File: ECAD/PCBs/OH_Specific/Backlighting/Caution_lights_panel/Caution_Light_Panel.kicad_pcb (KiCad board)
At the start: 2 copper layers, 81.9 x 39.8 mm, 31 parts, among them J1 Conn_01x04_Female, J2 Conn_01x04_Female

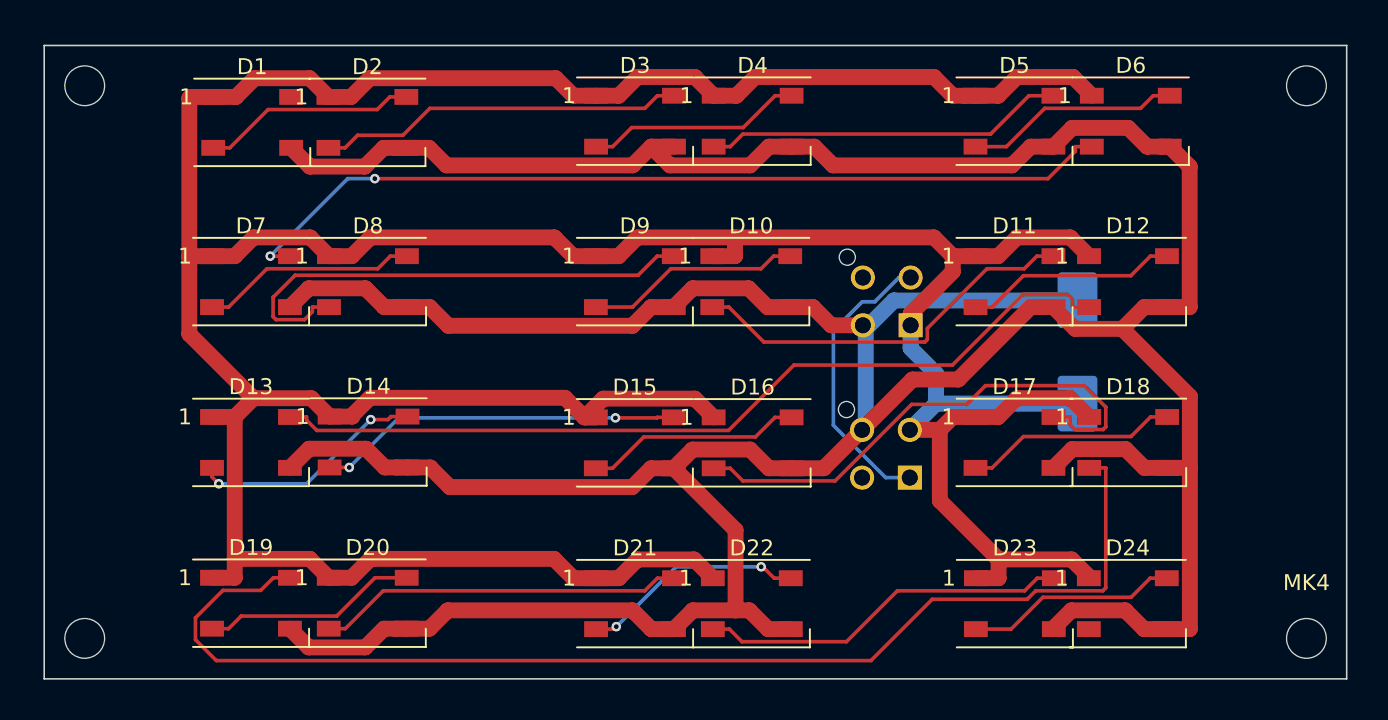
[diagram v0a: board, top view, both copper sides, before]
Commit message: Defog Lever Backlighting
Added - Degfog Lever PCB ECAD Files
Added - Defog Lever PCB MCAD Model
Added - Holes in the backplate for the backlighting LEDs
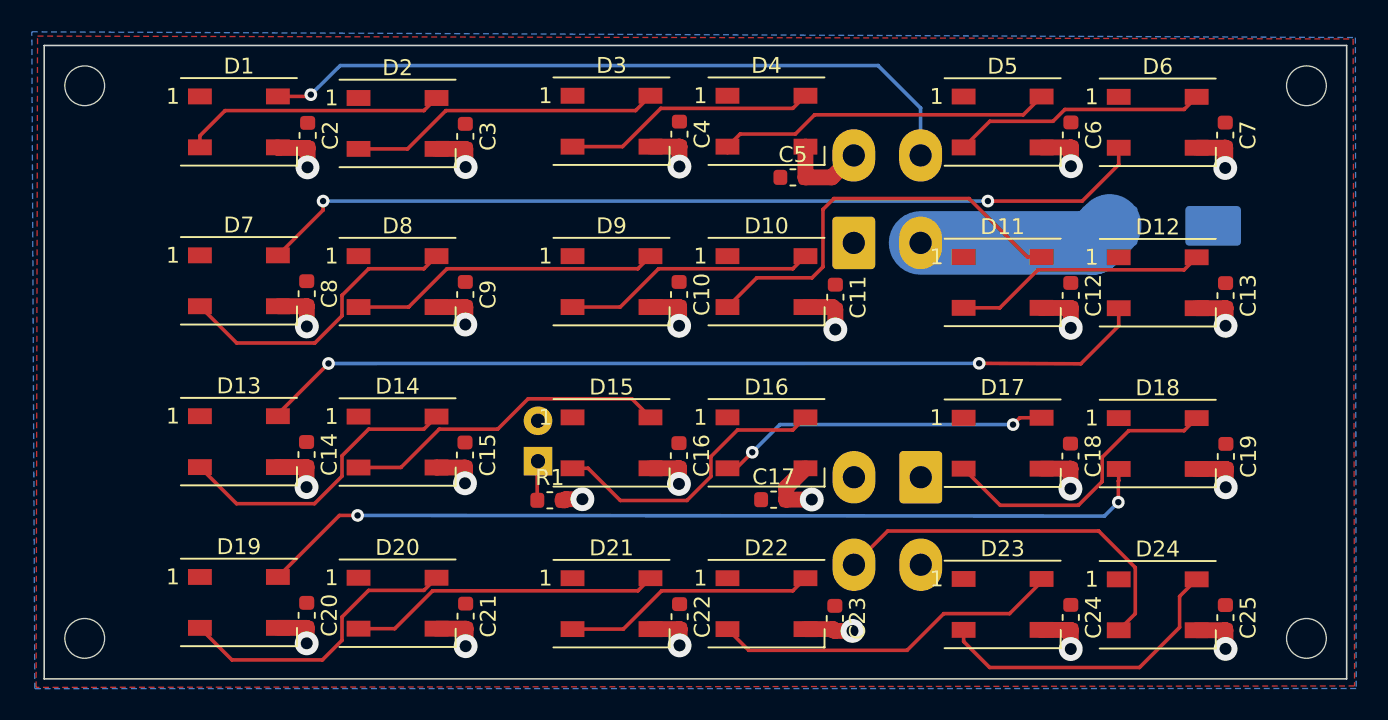
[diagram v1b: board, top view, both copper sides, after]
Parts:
- added C10: C, Capacitor_SMD:C_0603_1608Metric, F.Cu at (146.6, 85.7)
- added C11: C, Capacitor_SMD:C_0603_1608Metric, F.Cu at (156.4, 85.9)
- added C12: C, Capacitor_SMD:C_0603_1608Metric, F.Cu at (171.2, 85.8)
- added C13: C, Capacitor_SMD:C_0603_1608Metric, F.Cu at (180.9, 85.8)
- added C14: C, Capacitor_SMD:C_0603_1608Metric, F.Cu at (123.1, 95.8)
- added C15: C, Capacitor_SMD:C_0603_1608Metric, F.Cu at (133.1, 95.8)
- added C16: C, Capacitor_SMD:C_0603_1608Metric, F.Cu at (146.6, 95.9)
- added C17: C, Capacitor_SMD:C_0603_1608Metric, F.Cu at (152.5, 98.6)
- added C18: C, Capacitor_SMD:C_0603_1608Metric, F.Cu at (171.2, 95.9)
- added C19: C, Capacitor_SMD:C_0603_1608Metric, F.Cu at (180.9, 95.9)
- added C2: C, Capacitor_SMD:C_0603_1608Metric, F.Cu at (123.2, 75.7)
- added C20: C, Capacitor_SMD:C_0603_1608Metric, F.Cu at (123.2, 105.9)
- added C21: C, Capacitor_SMD:C_0603_1608Metric, F.Cu at (133.1, 105.9)
- added C22: C, Capacitor_SMD:C_0603_1608Metric, F.Cu at (146.6, 106.0)
- added C23: C, Capacitor_SMD:C_0603_1608Metric, F.Cu at (156.3, 106.1)
- added C24: C, Capacitor_SMD:C_0603_1608Metric, F.Cu at (171.2, 106.0)
- added C25: C, Capacitor_SMD:C_0603_1608Metric, F.Cu at (180.9, 106.0)
- added C3: C, Capacitor_SMD:C_0603_1608Metric, F.Cu at (133.1, 75.8)
- added C4: C, Capacitor_SMD:C_0603_1608Metric, F.Cu at (146.6, 75.6)
- added C5: C, Capacitor_SMD:C_0603_1608Metric, F.Cu at (153.7, 78.4)
- added C6: C, Capacitor_SMD:C_0603_1608Metric, F.Cu at (171.2, 75.7)
- added C7: C, Capacitor_SMD:C_0603_1608Metric, F.Cu at (180.9, 75.7)
- added C8: C, Capacitor_SMD:C_0603_1608Metric, F.Cu at (123.2, 85.7)
- added C9: C, Capacitor_SMD:C_0603_1608Metric, F.Cu at (133.1, 85.7)
- added D25: LED, LED_THT:LED_D3.0mm, B.Cu at (137.7, 96.2)
- added G***: LOGO, OH_General:CC-BY-NC-SA-Small, B.Cu at (132.3, 101.7)
- added G***: LOGO, OH_General:OH_LOGO_37.7mm_5.9mm, B.Cu at (132.2, 83.7)
- added R1: R, Resistor_SMD:R_0603_1608Metric, F.Cu at (138.4, 98.7)
- J1, J2: footprint footprints:Molex_MicroFit_2X2 -> Connector_Molex:Molex_Mini-Fit_Jr_5566-04A_2x02_P4.20mm_Vertical
- moved C1 9.52 mm to (176.9, 81.4), turned to 0 degrees
- moved J1 6.29 mm to (157.5, 82.5), turned to 0 degrees
- moved D2 1.90 mm to (128.9, 75.0)
- moved D24 1.88 mm to (176.6, 105.2)
- moved D20 1.87 mm to (128.9, 105.1)
- moved D12 1.87 mm to (176.6, 85.0)
- moved D8 1.86 mm to (128.9, 84.9)
- moved D18 1.86 mm to (176.6, 95.1)
- moved D14 1.82 mm to (128.9, 95.0)
- moved D6 1.69 mm to (176.6, 74.9)
- moved D21 1.48 mm to (142.3, 105.2)
- moved D3 1.48 mm to (142.3, 74.8)
- moved D9 1.47 mm to (142.3, 84.9)
- moved D15 1.47 mm to (142.3, 95.0)
- moved D10 0.96 mm to (152.1, 84.9)
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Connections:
- net Net-(D12-Pad2) renamed /DATAOUT1
- D1 pad 4: Net-(D1-Pad4) -> /DATAIN
- D24 pad 2: Net-(D24-Pad2) -> /DATAOUT
- J1 pad 2: /DATALOOP -> /LED+5V
- J2 pad 1: /DATALOOP -> /LED+5V
- J2 pad 3: /DATAOUT -> /LEDGND
- J2 pad 4: /LEDGND -> /DATAOUT
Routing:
- net /LED+5V: track 277.8 -> 12.3 mm
- net /LEDGND: track 281.9 -> 76.8 mm, vias 0 -> 24
- net /DATAIN: track 0.00 -> 45.3 mm, vias 0 -> 1
- net /DATAOUT: track 0.00 -> 23.9 mm
- net Net-(D18-Pad2): track 76.6 -> 57.0 mm, vias 0 -> 2
- net /DATALOOP: track 18.4 -> 0.00 mm
- net Net-(D16-Pad2): track 33.2 -> 21.1 mm, vias 0 -> 2
- net Net-(D8-Pad2): track 31.6 -> 19.7 mm
- net Net-(D23-Pad2): track 13.3 -> 19.5 mm
- net Net-(D17-Pad2): track 13.4 -> 18.8 mm
- net Net-(D7-Pad2): track 13.6 -> 18.8 mm
- net Net-(D19-Pad2): track 13.6 -> 18.7 mm
- net Net-(D15-Pad2): track 13.6 -> 18.4 mm
- net Net-(D13-Pad2): track 14.8 -> 18.8 mm, vias 2 -> 0
- net Net-(D20-Pad2): track 23.0 -> 19.7 mm
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- added copper zone on F.Cu, net /LED+5V
- added copper zone on B.Cu, net /LEDGND
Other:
- net class Default: via_dia 0.6 -> 0.8
- board text added: "Caution Lights Panel Designed by L. Walker"
- board text added: "Molex 2X2 Mini-Fit Jr."
- board text added: "READY"
- board text added: "Version 2.0"
- board text removed: "F/A 18C Simulator Caution Lights Panel Designed & Assembled in Australia © L. Walker 2021"
- board text removed: "Molex 2X2 MICRO-FIT"

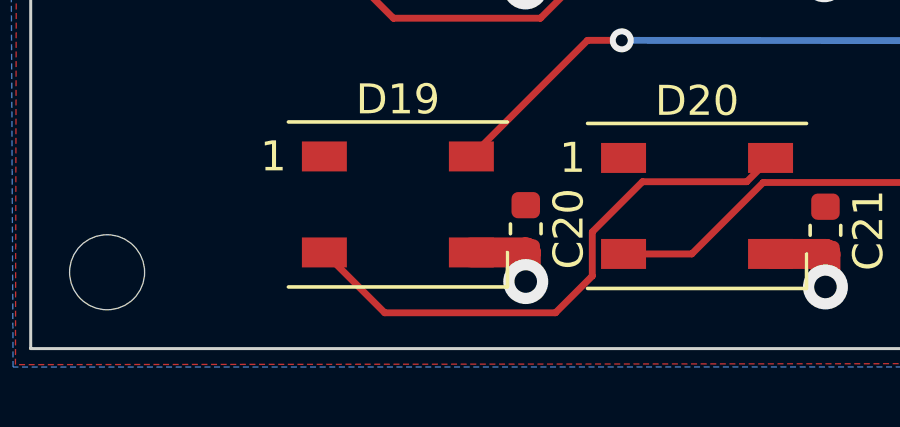
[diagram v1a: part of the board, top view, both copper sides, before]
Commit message: Latest backlighting changes
Update to multiple PCBs, mainly changing from micro-fit to mini-fit connectors.
Also changing from individual power rails to filled copper planes where possible.
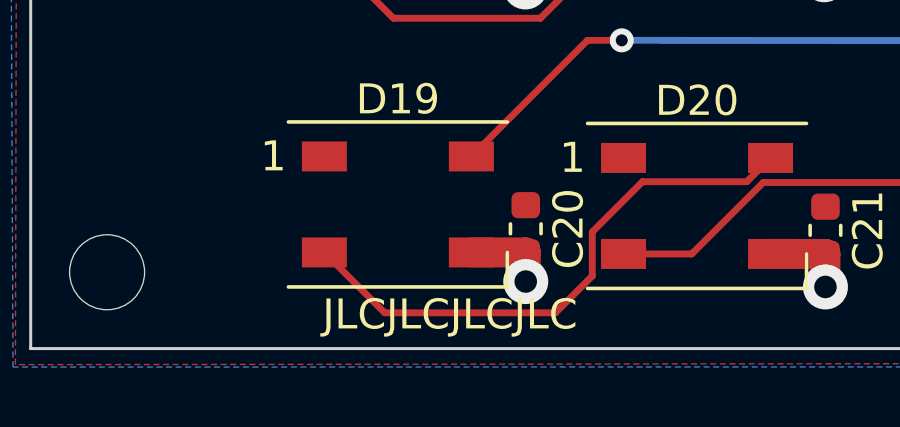
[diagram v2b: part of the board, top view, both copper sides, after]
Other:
- board text added: "JLCJLCJLCJLC"
